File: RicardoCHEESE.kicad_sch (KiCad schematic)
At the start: 37 parts, among them J1 RBUS, U1 ESP32-S3, Y1 40MHz±10ppm

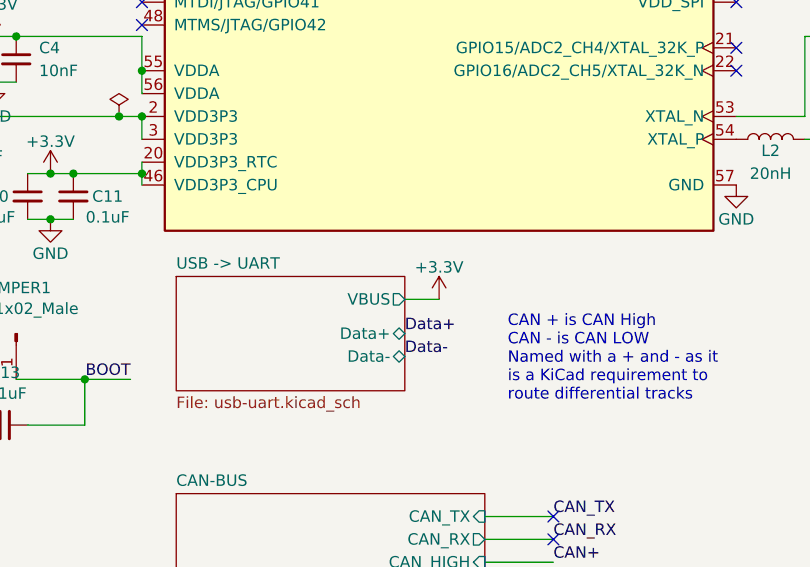
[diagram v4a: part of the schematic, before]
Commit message: Camera buck changes, c and r footprints, other
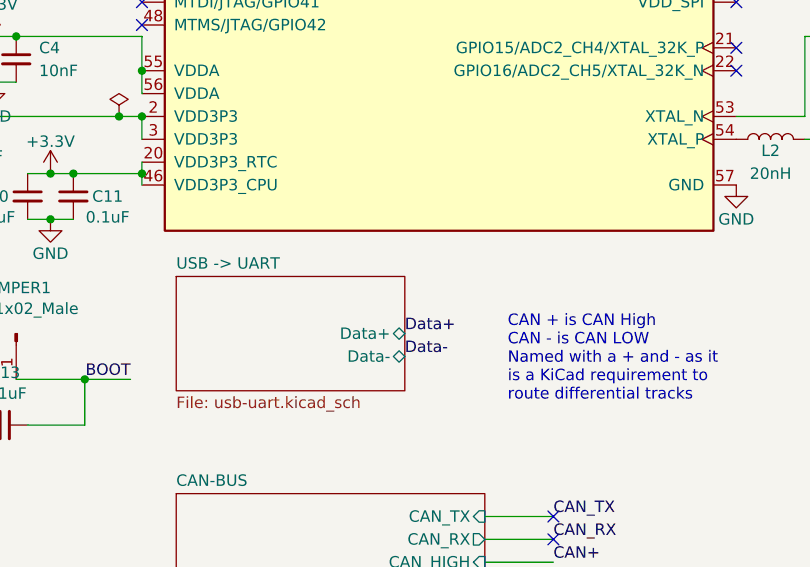
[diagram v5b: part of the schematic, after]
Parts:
- C14, C3, C5, C6: footprint Capacitor_SMD:C_0603_1608Metric -> Capacitor_SMD:C_0402_1005Metric
- C2, C9: footprint Capacitor_SMD:C_0201_0603Metric -> Capacitor_SMD:C_0402_1005Metric
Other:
- sheet USB -> UART ports: added none; removed VBUS
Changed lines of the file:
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@@
-    (stroke (width 0) (type default))
-  )
-  (wire (pts (xy 99.06 156.21) (xy 102.87 156.21))
     (stroke (width 0) (type default))
   )
@@
       (effects (font (size 1.27 1.27)))
     )
-    (property "Footprint" "Capacitor_SMD:C_0603_1608Metric" (at 22.86 191.77 0)
+    (property "Footprint" "Capacitor_SMD:C_0402_1005Metric" (at 22.86 191.77 0)
       (effects (font (size 1.27 1.27)) hide)
     )
@@
         (path "/7db990e4-92e1-4f99-b4d2-435bbec1ba83"
           (reference "BOOTJUMPER1") (unit 1)
-        )
-      )
-    )
-  )
-  (symbol (lib_id "power:+3.3V") (at 102.87 156.21 0) (unit 1)
-    (in_bom yes) (on_board yes) (dnp no)
-    (property "Reference" "#PWR018" (at 102.87 160.02 0)
-      (effects (font (size 1.27 1.27)) hide)
-    )
-    (property "Value" "+3.3V" (at 102.87 152.654 0)
-      (effects (font (size 1.27 1.27)))
-    )
-    (property "Footprint" "" (at 102.87 156.21 0)
-      (effects (font (size 1.27 1.27)) hide)
-    )
-    (property "Datasheet" "" (at 102.87 156.21 0)
-      (effects (font (size 1.27 1.27)) hide)
-    )
-    (pin "1")
-    (instances
-      (project "RicardoCHEESE"
-        (path "/7db990e4-92e1-4f99-b4d2-435bbec1ba83"
-          (reference "#PWR018") (unit 1)
         )
       )
@@
       (effects (font (size 1.27 1.27)) (justify left))
     )
-    (property "Footprint" "Capacitor_SMD:C_0603_1608Metric" (at 50.8 129.54 0)
+    (property "Footprint" "Capacitor_SMD:C_0402_1005Metric" (at 50.8 129.54 0)
       (effects (font (size 1.27 1.27)) hide)
     )
@@
       (effects (font (size 1.27 1.27)) (justify left))
     )
-    (property "Footprint" "Capacitor_SMD:C_0603_1608Metric" (at 20.32 138.43 0)
+    (property "Footprint" "Capacitor_SMD:C_0402_1005Metric" (at 20.32 138.43 0)
       (effects (font (size 1.27 1.27)) hide)
     )
@@
       (effects (font (size 1.27 1.27)) (justify left))
     )
-    (property "Footprint" "Capacitor_SMD:C_0201_0603Metric" (at 163.83 138.43 0)
+    (property "Footprint" "Capacitor_SMD:C_0402_1005Metric" (at 163.83 138.43 0)
       (effects (font (size 1.27 1.27)) hide)
     )
@@
       (effects (font (size 1.27 1.27)) (justify left))
     )
-    (property "Footprint" "Capacitor_SMD:C_0201_0603Metric" (at 162.56 127 0)
+    (property "Footprint" "Capacitor_SMD:C_0402_1005Metric" (at 162.56 127 0)
       (effects (font (size 1.27 1.27)) hide)
     )
@@
       (effects (font (size 1.27 1.27)) (justify left))
     )
-    (property "Footprint" "Capacitor_SMD:C_0603_1608Metric" (at 29.21 138.43 0)
+    (property "Footprint" "Capacitor_SMD:C_0402_1005Metric" (at 29.21 138.43 0)
       (effects (font (size 1.27 1.27)) hide)
     )
@@
       (effects (font (size 1.27 1.27)) (justify left top))
     )
-    (pin "VBUS" output (at 99.06 156.21 0)
-      (effects (font (size 1.27 1.27)) (justify right))
-    )
     (pin "Data+" bidirectional (at 99.06 160.02 0)

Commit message: Footprinting and board outline
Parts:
- 3V3LED1: footprint LED_SMD:LED_0603_1608Metric -> LED_SMD:LED_0402_1005Metric
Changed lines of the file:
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@@
       (effects (font (size 1.27 1.27)))
     )
-    (property "Footprint" "LED_SMD:LED_0603_1608Metric" (at 54.61 21.59 90)
+    (property "Footprint" "LED_SMD:LED_0402_1005Metric" (at 54.61 21.59 90)
       (effects (font (size 1.27 1.27)) hide)
     )

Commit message: Finished routing
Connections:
- net CAN_RX: now also U1.30 (SPIHD/GPIO27)
- net CAN_TX: now also U1.42 (GPIO37)
- no-connect marks 26 -> 22
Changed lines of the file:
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@@
   (junction (at 69.85 135.89) (diameter 0) (color 0 0 0 0)
   )
-  (no_connect (at 135.89 80.01))
   (no_connect (at 69.85 125.73))
   (no_connect (at 135.89 77.47))
   (no_connect (at 135.89 69.85))
   (no_connect (at 135.89 107.95))
-  (no_connect (at 115.57 182.88))
   (no_connect (at 135.89 87.63))
   (no_connect (at 135.89 115.57))
@@
   (no_connect (at 135.89 85.09))
   (no_connect (at 135.89 123.19))
-  (no_connect (at 135.89 105.41))
-  (no_connect (at 115.57 180.34))
   (wire (pts (xy 30.48 191.77) (xy 30.48 190.5))
     (stroke (width 0) (type default))
@@
     (stroke (width 0) (type default))
   )
+  (wire (pts (xy 135.89 80.01) (xy 139.7 80.01))
+    (stroke (width 0) (type default))
+  )
   (polyline (pts (xy 90.17 78.74) (xy 68.58 78.74))
     (stroke (width 0) (type default))
@@
     (stroke (width 0) (type default))
   )
+  (wire (pts (xy 135.89 105.41) (xy 140.335 105.41))
+    (stroke (width 0) (type default))
+  )
   (wire (pts (xy 50.8 132.08) (xy 53.34 132.08))
     (stroke (width 0) (type default))
@@
   )
   (wire (pts (xy 58.42 97.79) (xy 69.85 97.79))
+    (stroke (width 0) (type default))
+  )
+  (wire (pts (xy 140.335 105.41) (xy 140.335 106.68))
     (stroke (width 0) (type default))
   )
@@
     (effects (font (size 1.27 1.27)) (justify left bottom))
   )
+  (label "CAN_TX" (at 140.335 106.68 0) (fields_autoplaced)
+    (effects (font (size 1.27 1.27)) (justify left bottom))
+  )
   (label "Data+" (at 99.06 160.02 0) (fields_autoplaced)
     (effects (font (size 1.27 1.27)) (justify left bottom))
@@
     (effects (font (size 1.27 1.27)) (justify left bottom))
   )
+  (label "CAN_RX" (at 139.7 80.01 0) (fields_autoplaced)
+    (effects (font (size 1.27 1.27)) (justify left bottom))
+  )

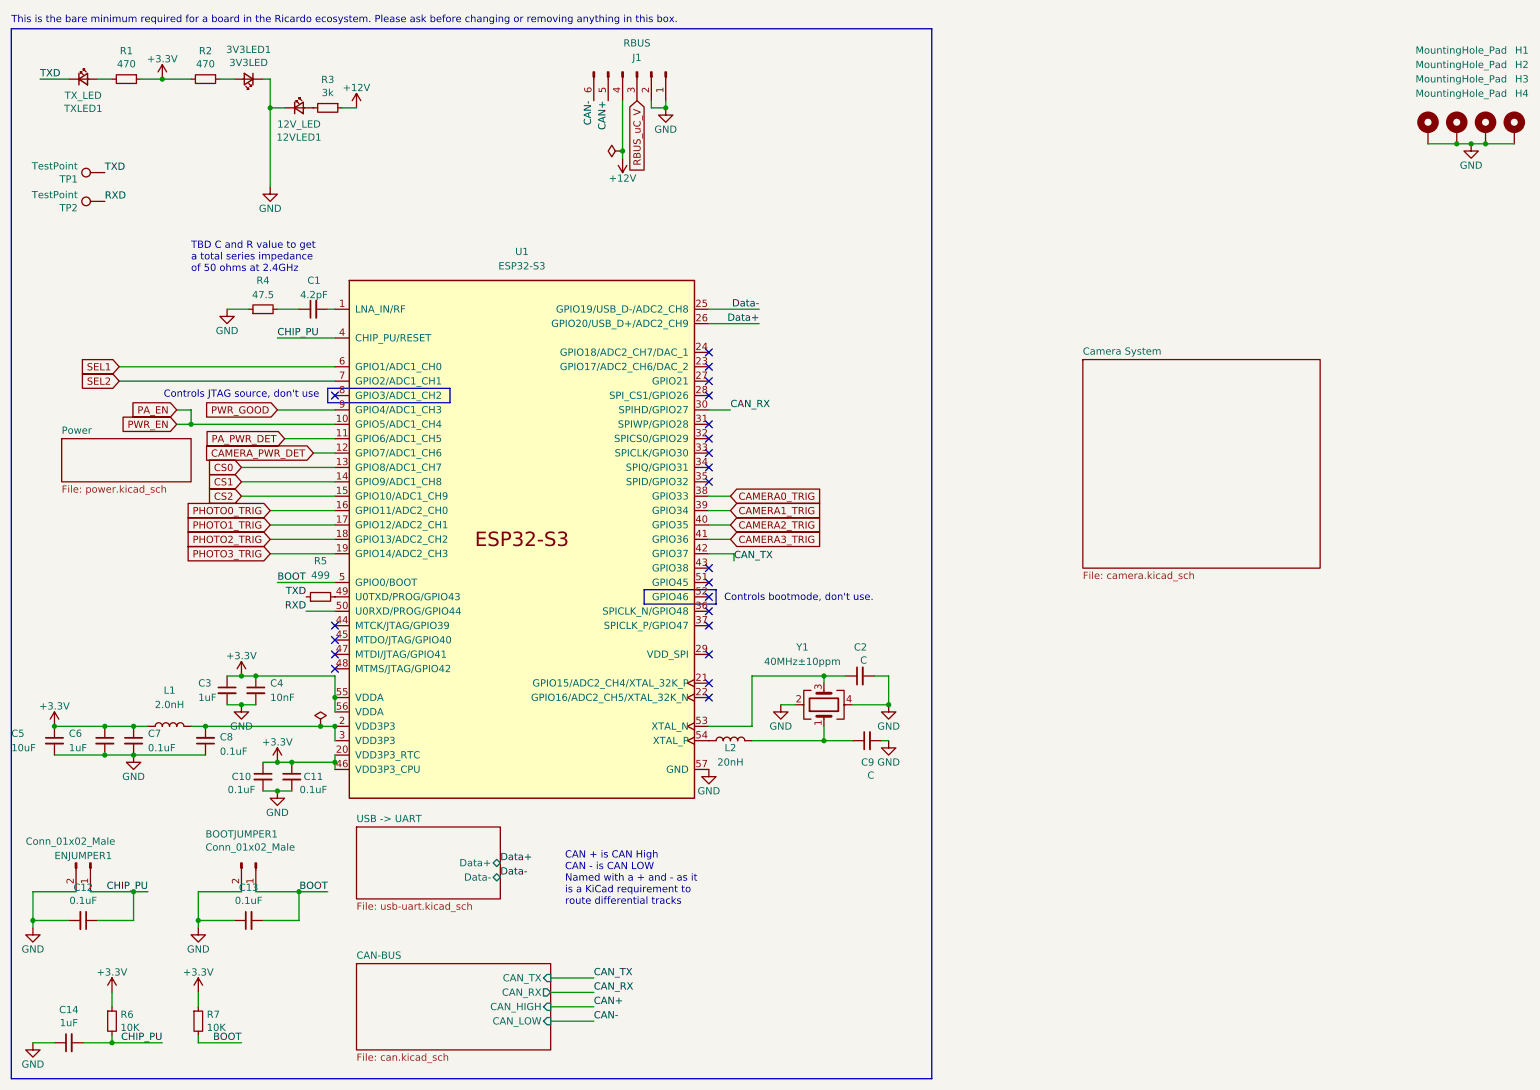
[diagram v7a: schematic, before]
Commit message: radio side needs reviewing
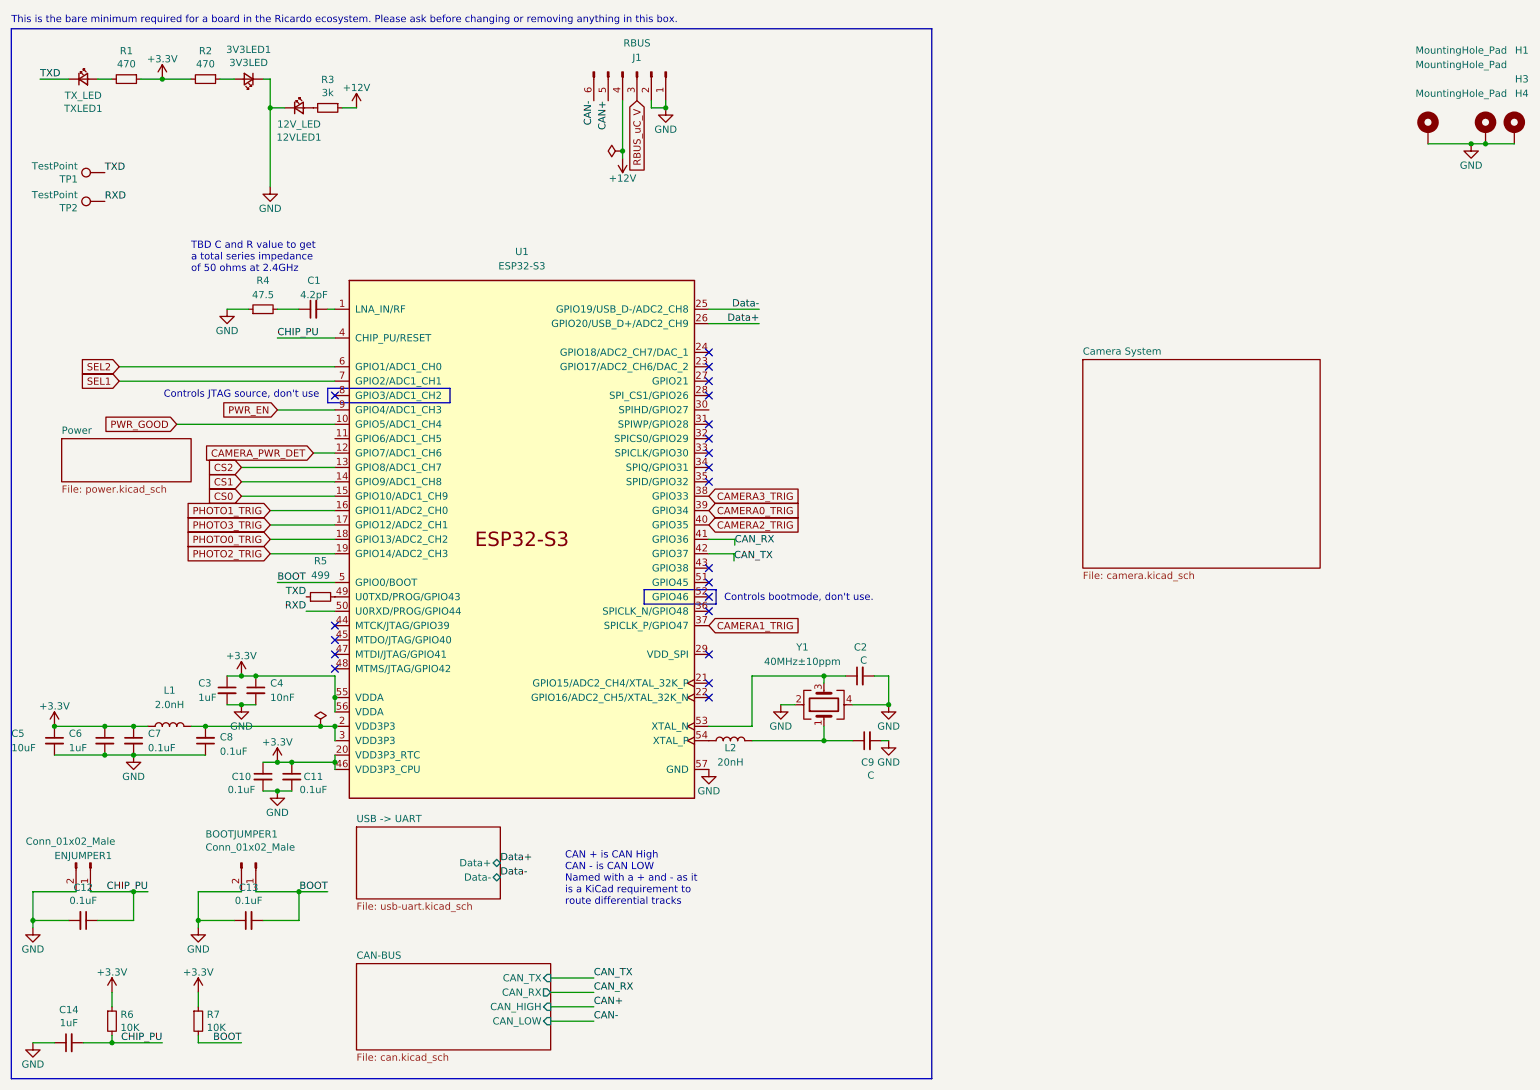
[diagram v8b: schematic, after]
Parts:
- removed H2: MountingHole_Pad, MountingHole:MountingHole_3.2mm_M3_DIN965_Pad, symbol Mechanical:MountingHole_Pad
- U1: footprint fps:QFN40P700X700X90-57N -> iclr:QFN40P700X700X90-57N
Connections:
- net PA_EN is gone; now on net PWR_GOOD: U1.10 (GPIO5/ADC1_CH4)
- net CAMERA0_TRIG: now also U1.39 (GPIO34); no longer U1.38 (GPIO33)
- net CAMERA1_TRIG: now also U1.37 (SPICLK_P/GPIO47); no longer U1.39 (GPIO34)
- net CAMERA3_TRIG: now also U1.38 (GPIO33); no longer U1.41 (GPIO36)
- net CAN_RX: now also U1.41 (GPIO36); no longer U1.30 (SPIHD/GPIO27)
- net CS0: now also U1.15 (GPIO10/ADC1_CH9); no longer U1.13 (GPIO8/ADC1_CH7)
- net CS2: now also U1.13 (GPIO8/ADC1_CH7); no longer U1.15 (GPIO10/ADC1_CH9)
- net PHOTO0_TRIG: now also U1.18 (GPIO13/ADC2_CH2); no longer U1.16 (GPIO11/ADC2_CH0)
- net PHOTO1_TRIG: now also U1.16 (GPIO11/ADC2_CH0); no longer U1.17 (GPIO12/ADC2_CH1)
- net PHOTO2_TRIG: now also U1.19 (GPIO14/ADC2_CH3); no longer U1.18 (GPIO13/ADC2_CH2)
- net PHOTO3_TRIG: now also U1.17 (GPIO12/ADC2_CH1); no longer U1.19 (GPIO14/ADC2_CH3)
- net PWR_GOOD: no longer U1.9 (GPIO4/ADC1_CH3)
- net SEL1: now also U1.7 (GPIO2/ADC1_CH1); no longer U1.6 (GPIO1/ADC1_CH0)
- net SEL2: now also U1.6 (GPIO1/ADC1_CH0); no longer U1.7 (GPIO2/ADC1_CH1)
- net PA_PWR_DET: no longer names the net of U1.11 (GPIO6/ADC1_CH5)
- new net PWR_EN: U1.9 (GPIO4/ADC1_CH3)
- no-connect marks 22 -> 21
